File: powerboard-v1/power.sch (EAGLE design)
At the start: 42 parts, among them IC1 IR4428S, IC2 AD7887ARZ, IC3 ADUM2401ARWZ, IC4 78L05SMD, IC5 7812, Q1 IRF1018E, Q2 IRF1018E

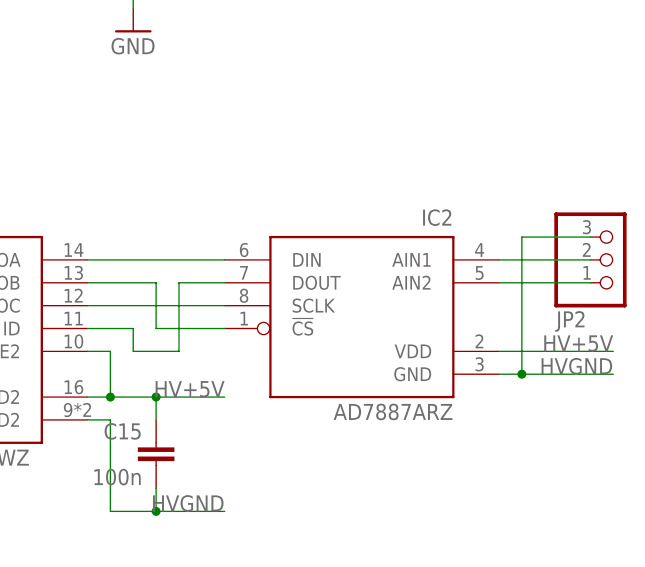
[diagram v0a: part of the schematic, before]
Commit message: Fix a mislabeled pin.
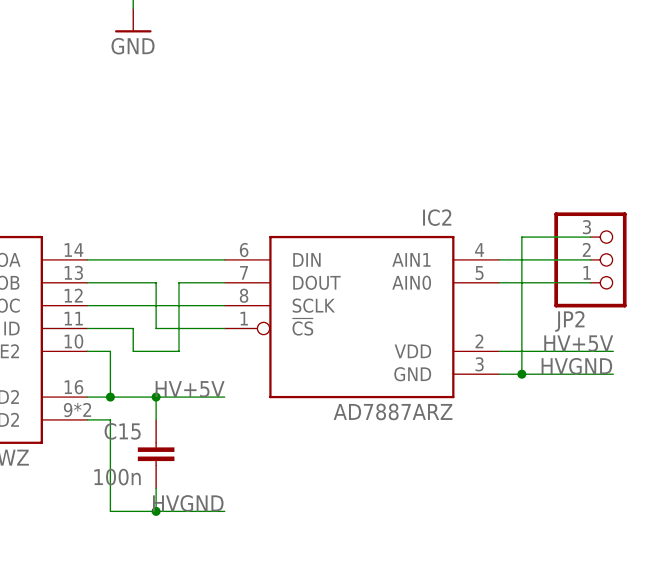
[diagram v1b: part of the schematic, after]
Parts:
- IC2: device local:AD7887ARZ -> 50w-modular-psu:AD7887ARZ
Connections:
- net N$15: now also IC2.AIN0; no longer IC2.AIN2
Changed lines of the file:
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@@
 <part name="C10" library="rcl" deviceset="CPOL-EU" device="B/3528-21R" value="10u"/>
 <part name="C8" library="rcl" deviceset="C-EU" device="C1206" value="100n"/>
-<part name="IC2" library="local" deviceset="AD7887" device="ARZ"/>
+<part name="IC2" library="50w-modular-psu" deviceset="AD7887" device="ARZ"/>
 <part name="IC3" library="local" deviceset="ADUM2401" device="RWZ" technology="A"/>
 <part name="C15" library="rcl" deviceset="C-EU" device="C1206" value="100n"/>
@@
 <net name="N$15" class="0">
 <segment>
-<pinref part="IC2" gate="G$1" pin="AIN2"/>
+<pinref part="IC2" gate="G$1" pin="AIN0"/>
 <wire x1="55.88" y1="-38.1" x2="66.04" y2="-38.1" width="0.1524" layer="91"/>
 <pinref part="JP2" gate="A" pin="1"/>

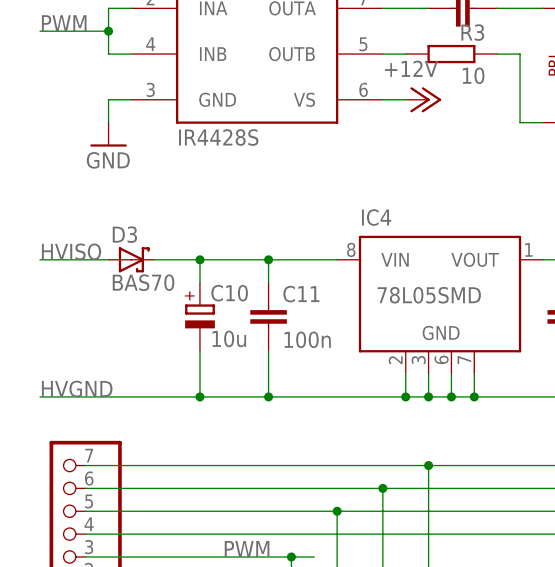
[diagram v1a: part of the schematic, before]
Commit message: D3: BAS70->BAS21.
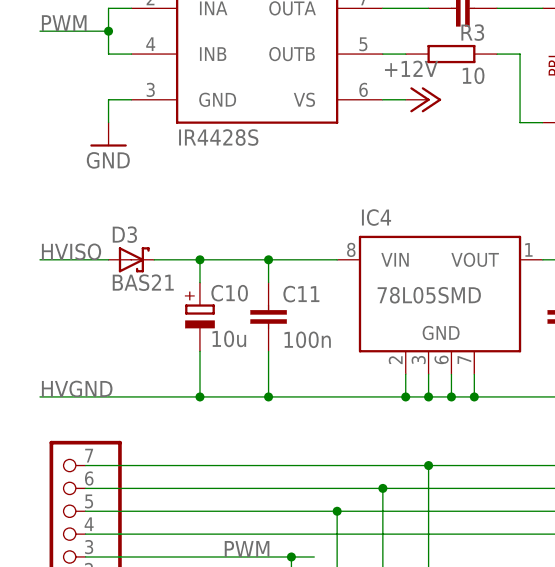
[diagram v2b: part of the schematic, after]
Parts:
- D3: value BAS70 -> BAS21
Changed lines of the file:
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@@
 <part name="GND3" library="supply1" deviceset="GND" device=""/>
 <part name="C2" library="rcl" deviceset="C-EU" device="C1206" value="100n"/>
-<part name="D3" library="diode" deviceset="BAS70" device=""/>
+<part name="D3" library="diode" deviceset="BAS70" device="" value="BAS21"/>
 <part name="C11" library="rcl" deviceset="C-EU" device="C1206" value="100n"/>
 <part name="C10" library="rcl" deviceset="CPOL-EU" device="B/3528-21R" value="10u"/>
